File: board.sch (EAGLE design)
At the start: 49 parts, among them IC1 ATMEGA48/88/168-AU, IC2 TP4056, IC3 MAX31865, Q1 IRFR5305

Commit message: cleanup of schematics
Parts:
- removed C9: 100n, rcl:C-EUC0603
- removed GND_LCD, SCL, SDA, VCC_LCD: (no value), wirepad:SMD2
- removed R12: 5.6k, rcl:R-EU_R0603
- removed RNTC: (no value), resistor:R-EU_R1206
- R11: value 10k -> 1,2k
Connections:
- net A3_NTC: no longer C9.2, R12.2, RNTC.2
- net A4_SDA: no longer SDA.P
- net A5_SCL: no longer SCL.P
- net GND: no longer C9.1, GND_LCD.P, R12.1
- net VCC: no longer RNTC.1, VCC_LCD.P
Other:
- note added: "Button"
- note added: "Charger"
- note added: "Heat control"
- note added: "LED connectors"
- note added: "Power Supply"
- note added: "Voltage Sensor"

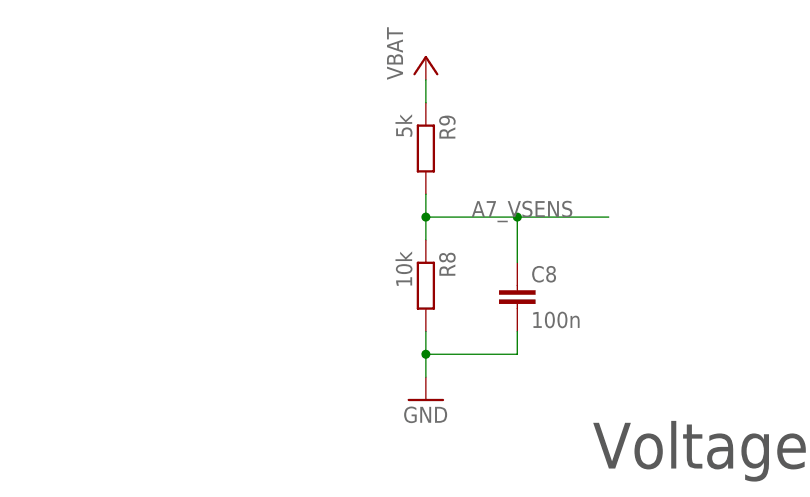
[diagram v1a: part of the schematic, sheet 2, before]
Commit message: using smaller resistors for voltage sensor
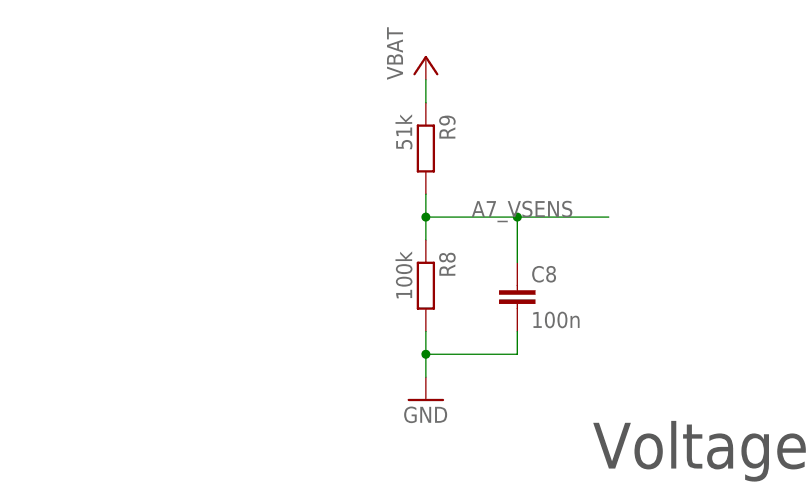
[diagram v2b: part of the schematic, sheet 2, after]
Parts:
- R8: value 10k -> 100k
- R9: value 5k -> 51k
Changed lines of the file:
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@@
 <part name="GND8" library="supply1" deviceset="GND" device=""/>
 <part name="R7" library="rcl" deviceset="R-EU_" device="R0603" value="100k"/>
-<part name="R8" library="rcl" deviceset="R-EU_" device="R0603" value="10k"/>
-<part name="R9" library="rcl" deviceset="R-EU_" device="R0603" value="5k"/>
+<part name="R8" library="rcl" deviceset="R-EU_" device="R0603" value="100k"/>
+<part name="R9" library="rcl" deviceset="R-EU_" device="R0603" value="51k"/>
 <part name="RAW2" library="supply1" deviceset="VCC" device="" value="VBAT"/>
 <part name="GND9" library="supply1" deviceset="GND" device=""/>

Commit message: using new mosfets, rearangement of parts
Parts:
- added Q2: IRLML2244, SparkFun-DiscreteSemi:MOSFET-PCHANNELIRLML2244
- added R4: 10k, rcl:R-EU_R0603
- Q1: value IRFR5305 -> PH2925U; device transistor-power:IRFR5305 -> selfmade:PH2925U
- R10: value 10k -> 100
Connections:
- net A3_NTC renamed A3
- net A4_SDA renamed A4
- net A5_SCL renamed A5
- new net GATE: Q1.G, R10.1, R7.2
- new net VCC_MAX: C5.1, IC3.DVDD, IC3.VDD, Q2.S
- net COIL: now also Q1.D; no longer Q1.S
- net D2_BUTTON: now also BTN1.P; no longer BTN2.P, R10.1
- net D3_GATE: now also R10.2; no longer Q1.G, R7.2
- net D8_VCC_MAX: now also Q2.G, R4.1; no longer C5.1, IC3.DVDD, IC3.VDD
- net GND: now also Q1.S, R4.2; no longer Q1.D, R10.2
- net VCC: now also Q2.D; no longer BTN1.P
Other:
- moved on the sheet: COIL, R10

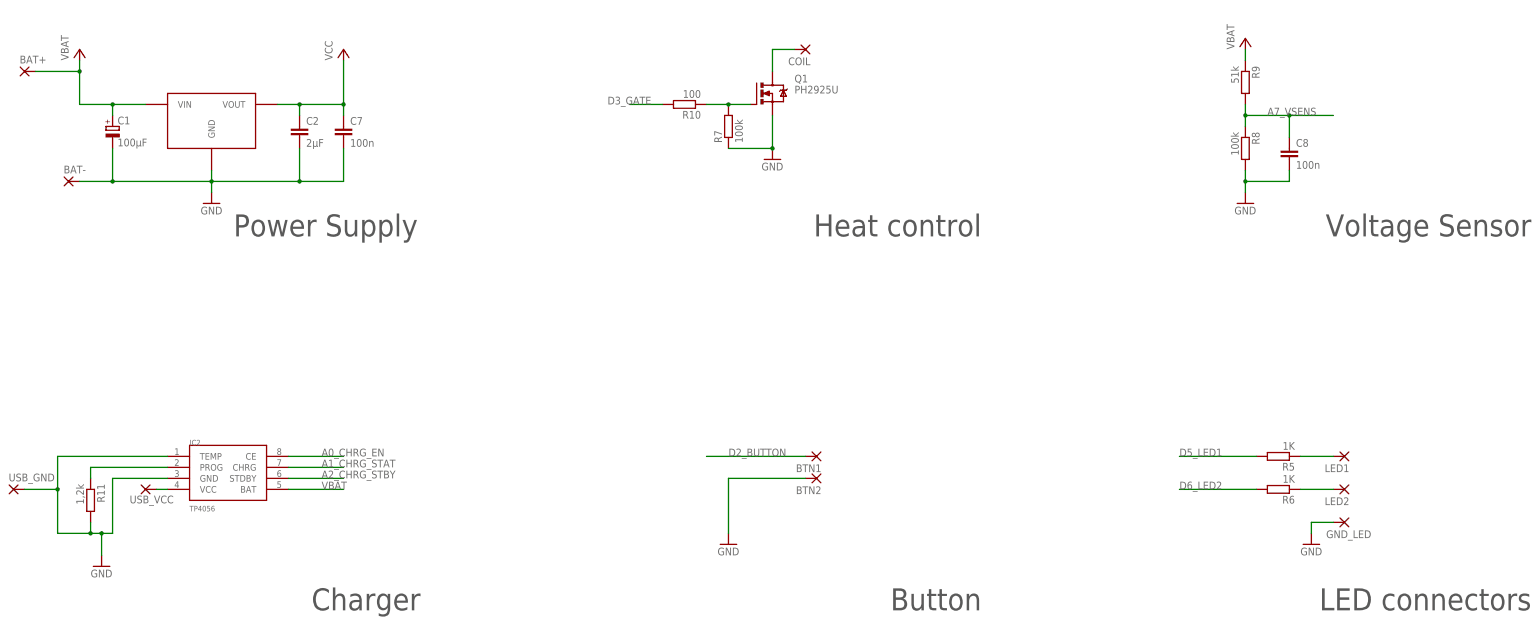
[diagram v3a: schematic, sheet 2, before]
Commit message: adding 3rd LED, new regulator, shrinking board
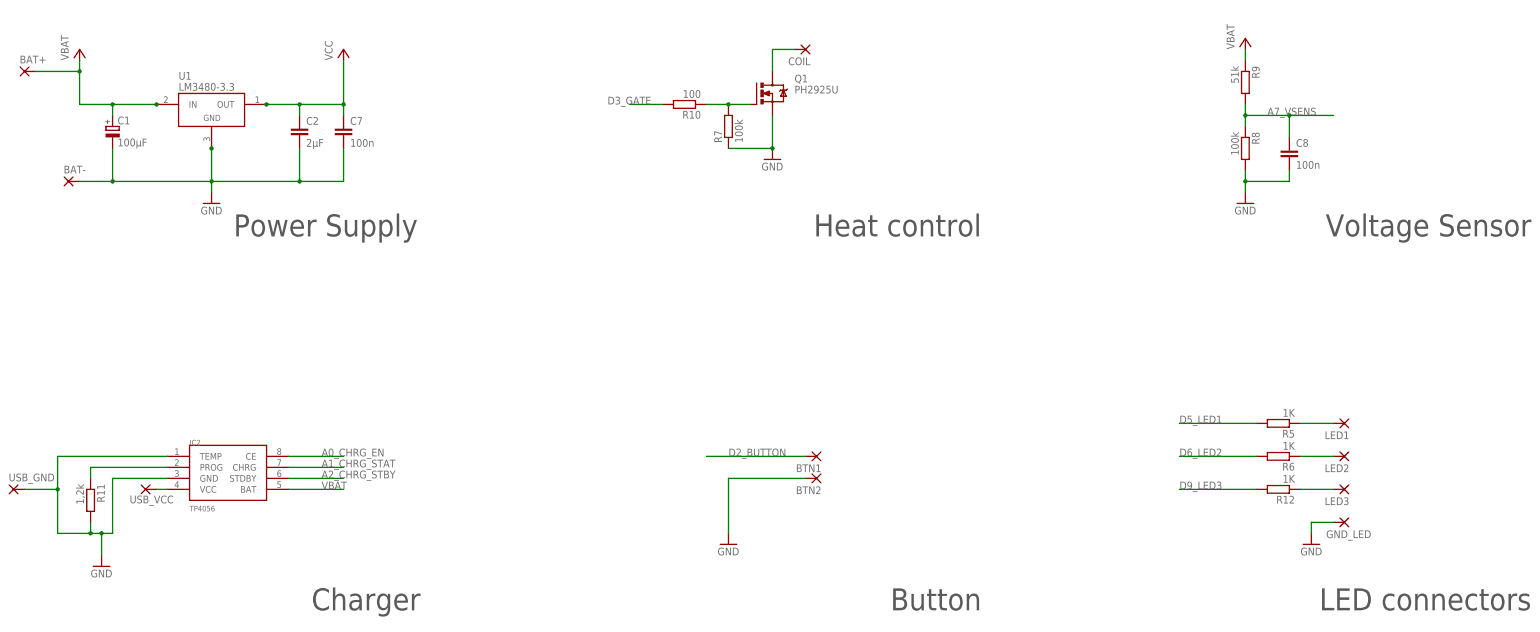
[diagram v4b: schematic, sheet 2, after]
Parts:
- removed U$2: TS9011, selfmade:TS9011
- added LED3: (no value), wirepad:SMD2
- added R12: 1K, rcl:R-EU_R0603
- added U1: LM3480-3.3, regulators:LM3480-3.3
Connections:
- removed net D9: IC1.PB1(OC1A/PCINT1)
- new net D9_LED3: IC1.PB1(OC1A/PCINT1), R12.2
- new net LED3: LED3.P, R12.1
- net GND: now also BTN2.P, U1.GND; no longer U$2.GND
- net VBAT: now also U1.IN; no longer U$2.VIN
- net VCC: now also U1.OUT; no longer U$2.VOUT
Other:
- moved on the sheet: LED1, LED2, R5, R6
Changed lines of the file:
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@@
 <?xml version="1.0" encoding="utf-8"?>
 <!DOCTYPE eagle SYSTEM "eagle.dtd">
-<eagle version="8.0.2">
+<eagle version="8.2.2">
 <drawing>
 <settings>
@@
 <part name="VBAT" library="supply1" deviceset="VCC" device="" value="VBAT"/>
 <part name="VCC" library="supply1" deviceset="VCC" device="" value="VCC"/>
-<part name="U$2" library="selfmade" deviceset="TS9011" device=""/>
 <part name="C1" library="resistor" deviceset="CPOL-EU" device="CT7343" value="100µF"/>
 <part name="C2" library="rcl" deviceset="C-EU" device="C1206" value="2µF"/>
@@
 <part name="R4" library="rcl" deviceset="R-EU_" device="R0603" value="10k"/>
 <part name="R10" library="rcl" deviceset="R-EU_" device="R0603" value="100"/>
+<part name="R12" library="rcl" deviceset="R-EU_" device="R0603" value="1K"/>
+<part name="LED3" library="wirepad" deviceset="SMD2" device=""/>
+<part name="U1" library="regulators" deviceset="LM3480-*" device="" technology="3.3"/>
 </parts>
 <sheets>
@@
 </segment>
 </net>
-<net name="D9" class="0">
+<net name="D9_LED3" class="0">
 <segment>
 <pinref part="IC1" gate="1" pin="PB1(OC1A/PCINT1)"/>
@@
 </segment>
 </net>
-<net name="D7" class="0">
-<segment>
-<pinref part="IC1" gate="1" pin="PD7(AIN1/PCINT23)"/>
-<wire x1="109.22" y1="71.12" x2="124.46" y2="71.12" width="0.1524" layer="91"/>
-<label x="114.3" y="71.12" size="1.778" layer="95"/>
-</segment>
-</net>
 <net name="A2_CHRG_STBY" class="0">
 <segment>
@@
 <wire x1="223.52" y1="111.76" x2="223.52" y2="121.92" width="0.1524" layer="91"/>
 <junction x="223.52" y="111.76"/>
+</segment>
+</net>
+<net name="D7" class="0">
+<segment>
+<pinref part="IC1" gate="1" pin="PD7(AIN1/PCINT23)"/>
+<wire x1="109.22" y1="71.12" x2="124.46" y2="71.12" width="0.1524" layer="91"/>
+<label x="114.3" y="71.12" size="1.778" layer="95"/>
 </segment>
 </net>
@@
 <instance part="VBAT" gate="VCC" x="33.02" y="149.86"/>
 <instance part="VCC" gate="VCC" x="93.98" y="149.86"/>
-<instance part="U$2" gate="G$1" x="63.5" y="132.08"/>
 <instance part="C1" gate="G$1" x="40.64" y="132.08"/>
 <instance part="C2" gate="G$1" x="83.82" y="132.08"/>
 <instance part="GND1" gate="1" x="63.5" y="114.3"/>
 <instance part="GND7" gate="1" x="317.5" y="35.56"/>
-<instance part="R5" gate="G$1" x="309.88" y="55.88" rot="R180"/>
-<instance part="R6" gate="G$1" x="309.88" y="48.26" rot="R180"/>
+<instance part="R5" gate="G$1" x="309.88" y="63.5" rot="R180"/>
+<instance part="R6" gate="G$1" x="309.88" y="55.88" rot="R180"/>
 <instance part="Q1" gate="G$1" x="190.5" y="139.7"/>
 <instance part="GND8" gate="1" x="193.04" y="124.46"/>
@@
 <instance part="GND11" gate="1" x="38.1" y="30.48"/>
 <instance part="R11" gate="G$1" x="35.56" y="45.72" rot="R270"/>
-<instance part="LED1" gate="1" x="325.12" y="55.88" rot="R180"/>
-<instance part="LED2" gate="1" x="325.12" y="48.26" rot="R180"/>
+<instance part="LED1" gate="1" x="325.12" y="63.5" rot="R180"/>
+<instance part="LED2" gate="1" x="325.12" y="55.88" rot="R180"/>
 <instance part="GND_LED" gate="1" x="325.12" y="40.64" smashed="yes" rot="R180">
 <attribute name="NAME" x="331.343" y="38.7858" size="1.778" layer="95" rot="R180"/>
@@
 <instance part="C8" gate="G$1" x="312.42" y="127"/>
 <instance part="R10" gate="G$1" x="172.72" y="137.16" rot="R180"/>
+<instance part="R12" gate="G$1" x="309.88" y="48.26" rot="R180"/>
+<instance part="LED3" gate="1" x="325.12" y="48.26" rot="R180"/>
+<instance part="U1" gate="G$1" x="63.5" y="137.16"/>
 </instances>
 <busses>
@@
 <net name="VCC" class="0">
 <segment>
-<pinref part="U$2" gate="G$1" pin="VOUT"/>
-<wire x1="78.74" y1="137.16" x2="83.82" y2="137.16" width="0.1524" layer="91"/>
+<wire x1="76.2" y1="137.16" x2="83.82" y2="137.16" width="0.1524" layer="91"/>
 <pinref part="C2" gate="G$1" pin="1"/>
 <wire x1="83.82" y1="137.16" x2="83.82" y2="134.62" width="0.1524" layer="91"/>
@@
 <wire x1="93.98" y1="137.16" x2="93.98" y2="134.62" width="0.1524" layer="91"/>
 <junction x="93.98" y="137.16"/>
+<pinref part="U1" gate="G$1" pin="OUT"/>
+<junction x="76.2" y="137.16"/>
 </segment>
 </net>
@@
 <wire x1="63.5" y1="119.38" x2="83.82" y2="119.38" width="0.1524" layer="91"/>
 <wire x1="83.82" y1="119.38" x2="83.82" y2="127" width="0.1524" layer="91"/>
-<pinref part="U$2" gate="G$1" pin="GND"/>
-<wire x1="63.5" y1="121.92" x2="63.5" y2="119.38" width="0.1524" layer="91"/>
+<wire x1="63.5" y1="127" x2="63.5" y2="119.38" width="0.1524" layer="91"/>
 <junction x="63.5" y="119.38"/>
 <pinref part="GND1" gate="1" pin="GND"/>
@@
 <wire x1="93.98" y1="119.38" x2="93.98" y2="127" width="0.1524" layer="91"/>
 <junction x="83.82" y="119.38"/>
+<pinref part="U1" gate="G$1" pin="GND"/>
+<junction x="63.5" y="127"/>
 </segment>
 <segment>
@@
 <wire x1="200.66" y1="50.8" x2="182.88" y2="50.8" width="0.1524" layer="91"/>
 <wire x1="182.88" y1="50.8" x2="182.88" y2="38.1" width="0.1524" layer="91"/>
+<pinref part="BTN2" gate="1" pin="P"/>
 </segment>
 <segment>
@@
 <segment>
 <pinref part="R6" gate="G$1" pin="1"/>
-<wire x1="314.96" y1="48.26" x2="322.58" y2="48.26" width="0.1524" layer="91"/>
+<wire x1="314.96" y1="55.88" x2="322.58" y2="55.88" width="0.1524" layer="91"/>
 <pinref part="LED2" gate="1" pin="P"/>
 </segment>
@@
 <segment>
 <pinref part="R5" gate="G$1" pin="2"/>
-<wire x1="304.8" y1="55.88" x2="287.02" y2="55.88" width="0.1524" layer="91"/>
-<label x="287.02" y="55.88" size="1.778" layer="95"/>
+<wire x1="304.8" y1="63.5" x2="287.02" y2="63.5" width="0.1524" layer="91"/>
+<label x="287.02" y="63.5" size="1.778" layer="95"/>
 </segment>
 </net>
@@
 </segment>
 <segment>
-<pinref part="U$2" gate="G$1" pin="VIN"/>
-<wire x1="48.26" y1="137.16" x2="40.64" y2="137.16" width="0.1524" layer="91"/>
+<wire x1="50.8" y1="137.16" x2="40.64" y2="137.16" width="0.1524" layer="91"/>
 <pinref part="C1" gate="G$1" pin="+"/>
 <wire x1="40.64" y1="137.16" x2="33.02" y2="137.16" width="0.1524" layer="91"/>
@@
 <wire x1="22.86" y1="144.78" x2="33.02" y2="144.78" width="0.1524" layer="91"/>
 <junction x="33.02" y="144.78"/>
+<pinref part="U1" gate="G$1" pin="IN"/>
+<junction x="50.8" y="137.16"/>
 </segment>
 </net>
@@
 <segment>
 <pinref part="R6" gate="G$1" pin="2"/>
-<wire x1="304.8" y1="48.26" x2="287.02" y2="48.26" width="0.1524" layer="91"/>
-<label x="287.02" y="48.26" size="1.778" layer="95"/>
+<wire x1="304.8" y1="55.88" x2="287.02" y2="55.88" width="0.1524" layer="91"/>
+<label x="287.02" y="55.88" size="1.778" layer="95"/>
 </segment>
 </net>
@@
 <pinref part="R5" gate="G$1" pin="1"/>
 <pinref part="LED1" gate="1" pin="P"/>
-<wire x1="314.96" y1="55.88" x2="322.58" y2="55.88" width="0.1524" layer="91"/>
+<wire x1="314.96" y1="63.5" x2="322.58" y2="63.5" width="0.1524" layer="91"/>
 </segment>
 </net>
@@
 </segment>
 </net>
+<net name="LED3" class="0">
+<segment>
+<pinref part="R12" gate="G$1" pin="1"/>
+<pinref part="LED3" gate="1" pin="P"/>
+<wire x1="322.58" y1="48.26" x2="314.96" y2="48.26" width="0.1524" layer="91"/>
+</segment>
+</net>
+<net name="D9_LED3" class="0">
+<segment>
+<pinref part="R12" gate="G$1" pin="2"/>
+<wire x1="304.8" y1="48.26" x2="287.02" y2="48.26" width="0.1524" layer="91"/>
+<label x="287.02" y="48.26" size="1.778" layer="95"/>
+</segment>
+</net>

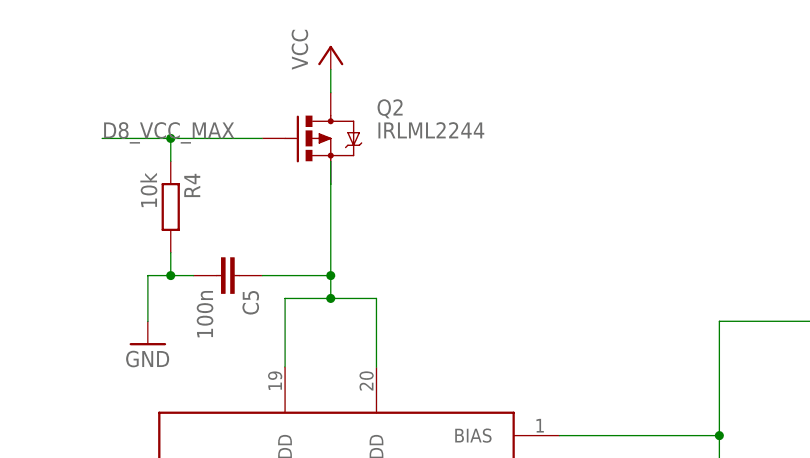
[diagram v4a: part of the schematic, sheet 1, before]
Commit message: using MCP1703 as vreg
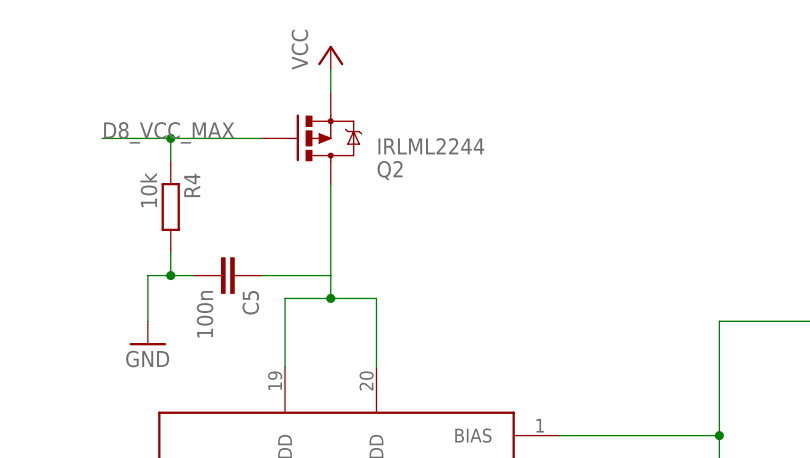
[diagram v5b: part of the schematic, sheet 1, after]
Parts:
- removed U1: LM3480-3.3, regulators:LM3480-3.3
- added IC4: MCP1703CB, linear:MCP1703CB
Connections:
- net GND: now also IC4.GND; no longer U1.GND
- net VBAT: now also IC4.VI; no longer U1.IN
- net VCC: now also IC4.VO, Q2.S; no longer Q2.D, U1.OUT
- net VCC_MAX: now also Q2.D; no longer Q2.S
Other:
- moved on the sheet: Q2
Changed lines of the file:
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@@
 <part name="R12" library="rcl" deviceset="R-EU_" device="R0603" value="1K"/>
 <part name="LED3" library="wirepad" deviceset="SMD2" device=""/>
-<part name="U1" library="regulators" deviceset="LM3480-*" device="" technology="3.3"/>
+<part name="IC4" library="linear" library_urn="urn:adsk.eagle:library:262" deviceset="MCP1703" device="CB"/>
 </parts>
 <sheets>
@@
 <instance part="GND14" gate="1" x="25.4" y="78.74"/>
 <instance part="C11" gate="G$1" x="30.48" y="91.44" rot="R90"/>
-<instance part="Q2" gate="G$1" x="223.52" y="127"/>
+<instance part="Q2" gate="G$1" x="223.52" y="127" rot="MR180"/>
 <instance part="VCC3" gate="VCC" x="223.52" y="137.16"/>
 <instance part="R4" gate="G$1" x="205.74" y="119.38" rot="R270"/>
@@
 </segment>
 <segment>
-<pinref part="Q2" gate="G$1" pin="D"/>
+<pinref part="Q2" gate="G$1" pin="S"/>
 <pinref part="VCC3" gate="VCC" pin="VCC"/>
-<wire x1="223.52" y1="134.62" x2="223.52" y2="132.08" width="0.1524" layer="91"/>
+<wire x1="223.52" y1="132.08" x2="223.52" y2="134.62" width="0.1524" layer="91"/>
 </segment>
 </net>
@@
 <wire x1="215.9" y1="111.76" x2="223.52" y2="111.76" width="0.1524" layer="91"/>
 <junction x="223.52" y="109.22"/>
-<wire x1="223.52" y1="121.92" x2="223.52" y2="124.46" width="0.1524" layer="91"/>
-<pinref part="Q2" gate="G$1" pin="S"/>
+<pinref part="Q2" gate="G$1" pin="D"/>
 <wire x1="223.52" y1="111.76" x2="223.52" y2="121.92" width="0.1524" layer="91"/>
-<junction x="223.52" y="111.76"/>
 </segment>
 </net>
@@
 <instance part="R12" gate="G$1" x="309.88" y="48.26" rot="R180"/>
 <instance part="LED3" gate="1" x="325.12" y="48.26" rot="R180"/>
-<instance part="U1" gate="G$1" x="63.5" y="137.16"/>
+<instance part="IC4" gate="G$1" x="63.5" y="137.16"/>
 </instances>
 <busses>
@@
 <net name="VCC" class="0">
 <segment>
-<wire x1="76.2" y1="137.16" x2="83.82" y2="137.16" width="0.1524" layer="91"/>
+<wire x1="73.66" y1="137.16" x2="83.82" y2="137.16" width="0.1524" layer="91"/>
 <pinref part="C2" gate="G$1" pin="1"/>
 <wire x1="83.82" y1="137.16" x2="83.82" y2="134.62" width="0.1524" layer="91"/>
@@
 <wire x1="93.98" y1="137.16" x2="93.98" y2="134.62" width="0.1524" layer="91"/>
 <junction x="93.98" y="137.16"/>
-<pinref part="U1" gate="G$1" pin="OUT"/>
-<junction x="76.2" y="137.16"/>
+<pinref part="IC4" gate="G$1" pin="VO"/>
 </segment>
 </net>
@@
 <wire x1="63.5" y1="119.38" x2="83.82" y2="119.38" width="0.1524" layer="91"/>
 <wire x1="83.82" y1="119.38" x2="83.82" y2="127" width="0.1524" layer="91"/>
-<wire x1="63.5" y1="127" x2="63.5" y2="119.38" width="0.1524" layer="91"/>
+<wire x1="63.5" y1="129.54" x2="63.5" y2="119.38" width="0.1524" layer="91"/>
 <junction x="63.5" y="119.38"/>
 <pinref part="GND1" gate="1" pin="GND"/>
@@
 <wire x1="93.98" y1="119.38" x2="93.98" y2="127" width="0.1524" layer="91"/>
 <junction x="83.82" y="119.38"/>
-<pinref part="U1" gate="G$1" pin="GND"/>
-<junction x="63.5" y="127"/>
+<pinref part="IC4" gate="G$1" pin="GND"/>
 </segment>
 <segment>
@@
 </segment>
 <segment>
-<wire x1="50.8" y1="137.16" x2="40.64" y2="137.16" width="0.1524" layer="91"/>
+<wire x1="53.34" y1="137.16" x2="40.64" y2="137.16" width="0.1524" layer="91"/>
 <pinref part="C1" gate="G$1" pin="+"/>
 <wire x1="40.64" y1="137.16" x2="33.02" y2="137.16" width="0.1524" layer="91"/>
@@
 <wire x1="22.86" y1="144.78" x2="33.02" y2="144.78" width="0.1524" layer="91"/>
 <junction x="33.02" y="144.78"/>
-<pinref part="U1" gate="G$1" pin="IN"/>
-<junction x="50.8" y="137.16"/>
+<pinref part="IC4" gate="G$1" pin="VI"/>
 </segment>
 </net>
@@
 </schematic>
 </drawing>
+<compatibility>
+<note version="8.2" severity="warning">
+Since Version 8.2, Eagle supports online libraries. The ids
+of those online libraries will not be understood (or retained)
+with this version.
+</note>
+</compatibility>
 </eagle>
